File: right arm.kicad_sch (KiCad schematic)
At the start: 11 parts, among them M13 Stepper_Motor_bipolar, M14 Motor_Servo, M15 Motor_Servo, M16 Motor_Servo, M17 Stepper_Motor_bipolar, M18 RHP020N06, M19 Motor_DC, M20 Stepper_Motor_bipolar

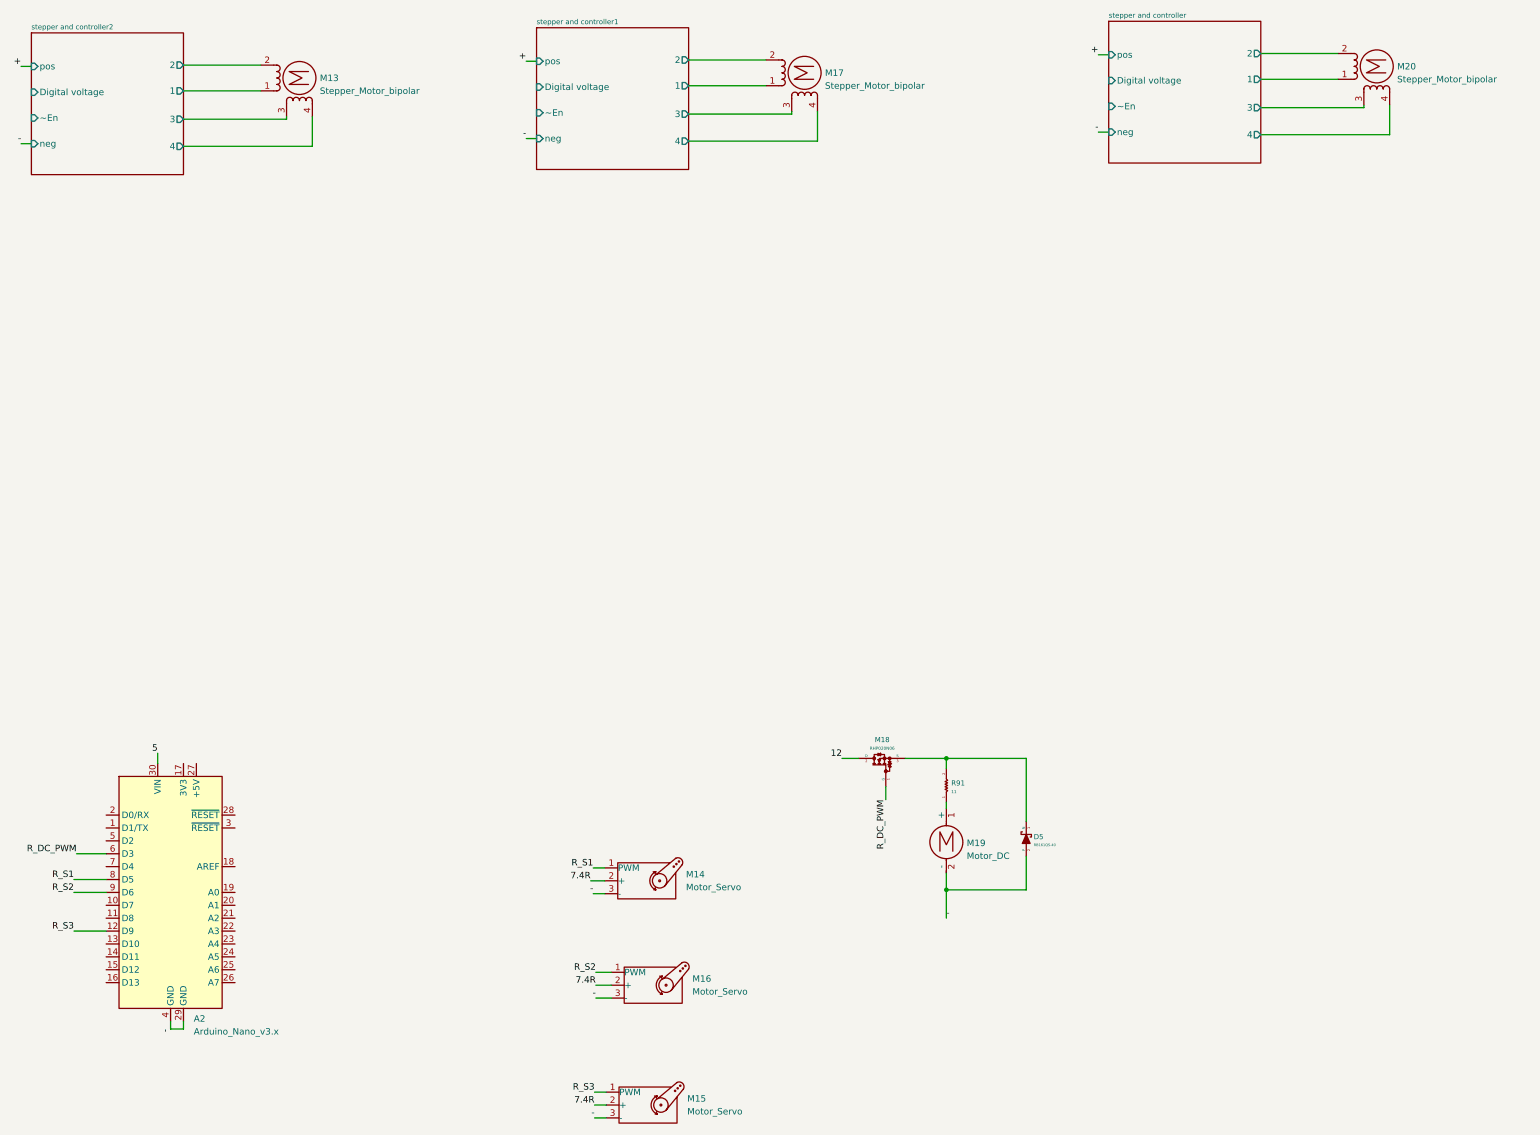
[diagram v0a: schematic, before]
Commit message: base schematic and PCB made
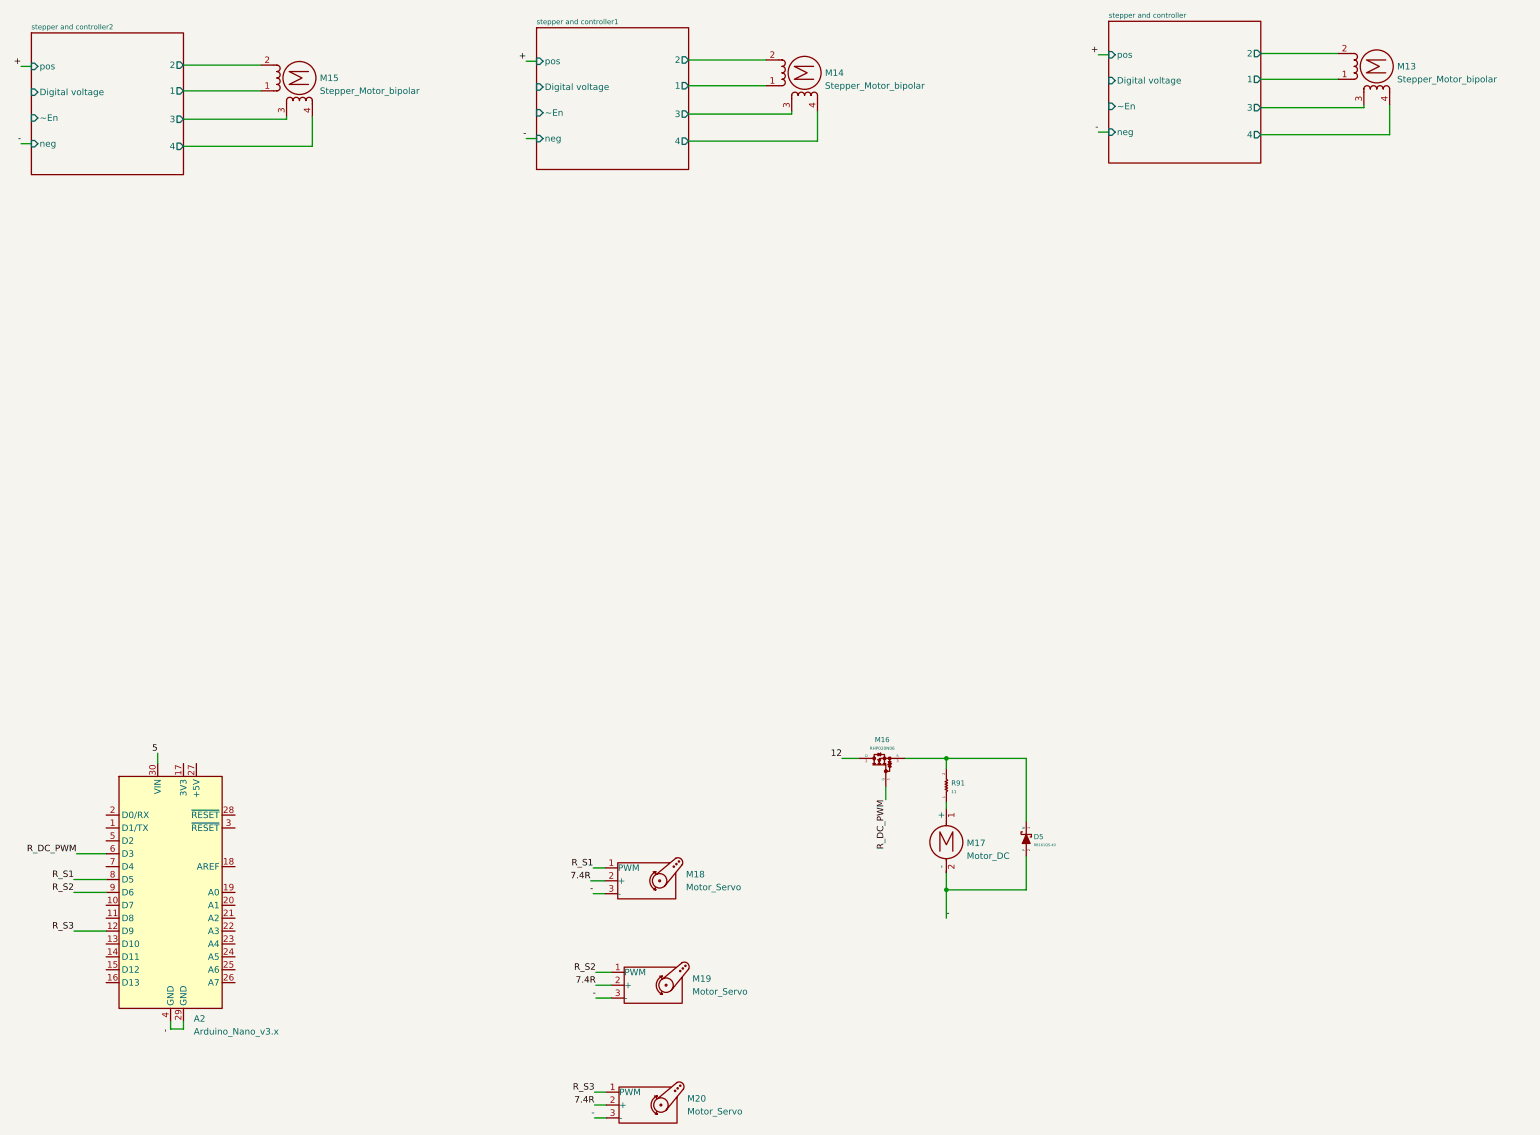
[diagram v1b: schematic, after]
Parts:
- D5: footprint my_footprints:RB161QS-40T18R -> Diodes:RB161QS-40T18R; symbol diodes:RB161QS-40 -> Diodes:RB161QS-40
- M13: renamed from M20; footprint (none) -> Connectors:1-350944-0
- M14: renamed from M17; footprint (none) -> Connectors:1-350944-0
- M15: renamed from M13; footprint (none) -> Connectors:1-350944-0
- M16: renamed from M18; footprint my_footprints:RHP020N06T100 -> E-MOSFETs:RHP020N06T100
- R91: footprint my_footprints:MCR03EZPFX -> Resistors:MCR03EZPFX; symbol resistors:MCR03EZPFX -> Resistors:MCR03EZPFX
- renumbered M19 to M17, M14 to M18, M16 to M19, M15 to M20
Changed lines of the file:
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@@
   (symbol (lib_id "E-MOSFETs:RHP020N06") (at 244.348 187.96 90) (unit 1)
     (in_bom yes) (on_board yes) (fields_autoplaced)
-    (property "Reference" "M18" (id 0) (at 244.9064 184.2844 90)
+    (property "Reference" "M16" (id 0) (at 244.9064 184.2844 90)
       (effects (font (size 1 1)))
     )
@@
       (effects (font (size 0.6 0.6)))
     )
-    (property "Footprint" "my_footprints:RHP020N06T100" (id 2) (at 259.842 187.96 0)
+    (property "Footprint" "E-MOSFETs:RHP020N06T100" (id 2) (at 259.842 187.96 0)
       (effects (font (size 1.524 1.524)) hide)
     )
@@
     (pin "9")
   )
-  (symbol (lib_id "resistors:MCR03EZPFX") (at 257.556 193.294 90) (unit 1)
+  (symbol (lib_id "Resistors:MCR03EZPFX") (at 257.556 193.294 90) (unit 1)
     (in_bom yes) (on_board yes) (fields_autoplaced)
     (property "Reference" "R91" (id 0) (at 258.5212 192.8327 90)
@@
       (effects (font (size 0.6 0.6)) (justify right))
     )
-    (property "Footprint" "my_footprints:MCR03EZPFX" (id 2) (at 265.43 193.294 0)
+    (property "Footprint" "Resistors:MCR03EZPFX" (id 2) (at 265.43 193.294 0)
       (effects (font (size 1.27 1.27)) hide)
     )
@@
   (symbol (lib_id "Motor:Stepper_Motor_bipolar") (at 342.392 51.562 90) (unit 1)
     (in_bom yes) (on_board yes) (fields_autoplaced)
-    (property "Reference" "M20" (id 0) (at 346.4052 51.5782 90)
+    (property "Reference" "M13" (id 0) (at 346.4052 51.5782 90)
       (effects (font (size 1.27 1.27)) (justify right))
     )
@@
       (effects (font (size 1.27 1.27)) (justify right))
     )
-    (property "Footprint" "" (id 2) (at 342.646 51.308 0)
+    (property "Footprint" "Connectors:1-350944-0" (id 2) (at 342.646 51.308 0)
       (effects (font (size 1.27 1.27)) hide)
     )
@@
   (symbol (lib_id "Motor:Stepper_Motor_bipolar") (at 130.048 53.848 90) (unit 1)
     (in_bom yes) (on_board yes) (fields_autoplaced)
-    (property "Reference" "M13" (id 0) (at 134.0612 53.8642 90)
+    (property "Reference" "M15" (id 0) (at 134.0612 53.8642 90)
       (effects (font (size 1.27 1.27)) (justify right))
     )
@@
       (effects (font (size 1.27 1.27)) (justify right))
     )
-    (property "Footprint" "" (id 2) (at 130.302 53.594 0)
+    (property "Footprint" "Connectors:1-350944-0" (id 2) (at 130.302 53.594 0)
       (effects (font (size 1.27 1.27)) hide)
     )
@@
     (pin "4")
   )
-  (symbol (lib_name "RB161QS-40_1") (lib_id "diodes:RB161QS-40") (at 273.304 203.962 270) (unit 1)
+  (symbol (lib_id "Diodes:RB161QS-40") (at 273.304 203.962 270) (unit 1)
     (in_bom yes) (on_board yes) (fields_autoplaced)
     (property "Reference" "D5" (id 0) (at 274.7772 203.4193 90)
@@
       (effects (font (size 0.5 0.5)) (justify left))
     )
-    (property "Footprint" "my_footprints:RB161QS-40T18R" (id 2) (at 262.636 203.962 0)
+    (property "Footprint" "Diodes:RB161QS-40T18R" (id 2) (at 262.636 203.962 0)
       (effects (font (size 1.524 1.524)) hide)
     )
@@
   (symbol (lib_id "Motor:Stepper_Motor_bipolar") (at 229.616 52.832 90) (unit 1)
     (in_bom yes) (on_board yes) (fields_autoplaced)
-    (property "Reference" "M17" (id 0) (at 233.6292 52.8482 90)
+    (property "Reference" "M14" (id 0) (at 233.6292 52.8482 90)
       (effects (font (size 1.27 1.27)) (justify right))
     )
@@
       (effects (font (size 1.27 1.27)) (justify right))
     )
-    (property "Footprint" "" (id 2) (at 229.87 52.578 0)
+    (property "Footprint" "Connectors:1-350944-0" (id 2) (at 229.87 52.578 0)
       (effects (font (size 1.27 1.27)) hide)
     )
@@
   (symbol (lib_id "Motor:Motor_Servo") (at 197.866 212.09 0) (unit 1)
     (in_bom yes) (on_board yes) (fields_autoplaced)
-    (property "Reference" "M14" (id 0) (at 206.2258 210.8219 0)
+    (property "Reference" "M18" (id 0) (at 206.2258 210.8219 0)
       (effects (font (size 1.27 1.27)) (justify left))
     )
@@
   (symbol (lib_id "Motor:Motor_DC") (at 257.556 202.946 0) (unit 1)
     (in_bom yes) (on_board yes) (fields_autoplaced)
-    (property "Reference" "M19" (id 0) (at 261.5692 204.6513 0)
+    (property "Reference" "M17" (id 0) (at 261.5692 204.6513 0)
       (effects (font (size 1.27 1.27)) (justify left))
     )
@@
   (symbol (lib_id "Motor:Motor_Servo") (at 199.136 232.664 0) (unit 1)
     (in_bom yes) (on_board yes) (fields_autoplaced)
-    (property "Reference" "M16" (id 0) (at 207.4958 231.3959 0)
+    (property "Reference" "M19" (id 0) (at 207.4958 231.3959 0)
       (effects (font (size 1.27 1.27)) (justify left))
     )
@@
   (symbol (lib_id "Motor:Motor_Servo") (at 198.12 256.286 0) (unit 1)
     (in_bom yes) (on_board yes) (fields_autoplaced)
-    (property "Reference" "M15" (id 0) (at 206.4798 255.0179 0)
-      (effects (font (size 1.27 1.27)) (justify left))
-    )
+    (property "Reference" "M20" (id 0) (at 206.4798 255.0179 0)
+      (effects (font (size 1.27 1.27)) (justify left))
+    )
